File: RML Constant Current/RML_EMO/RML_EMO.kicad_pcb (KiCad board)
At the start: 2 copper layers, 72 x 34 mm, 50 parts, among them J1 Tyco, J2 NANOFIT-4PIN, J3 Tyco, Q3 Q_NMOS_GSD, Q4 Q_NMOS_GSD, Q5 Q_NMOS_GSD, U1 LR8K4-G, U2 LM555xM, U5 LM1117DT-5.0, U6 Optocoupler, U7 74AHC1G02, U8 OPA1662DGK

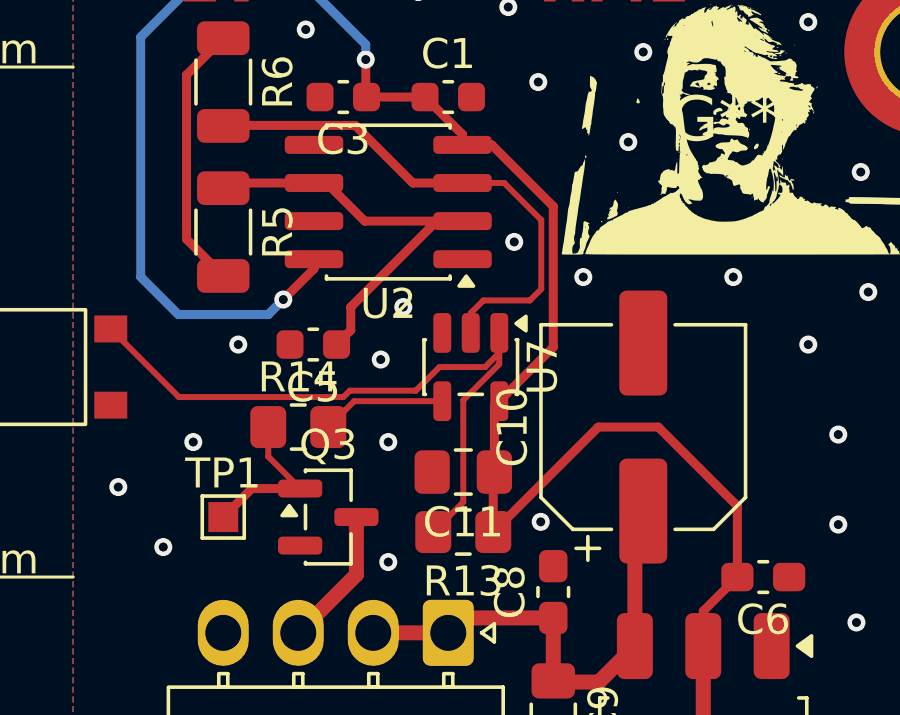
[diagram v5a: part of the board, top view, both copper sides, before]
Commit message: changed nor gate footprint to smaller footprint
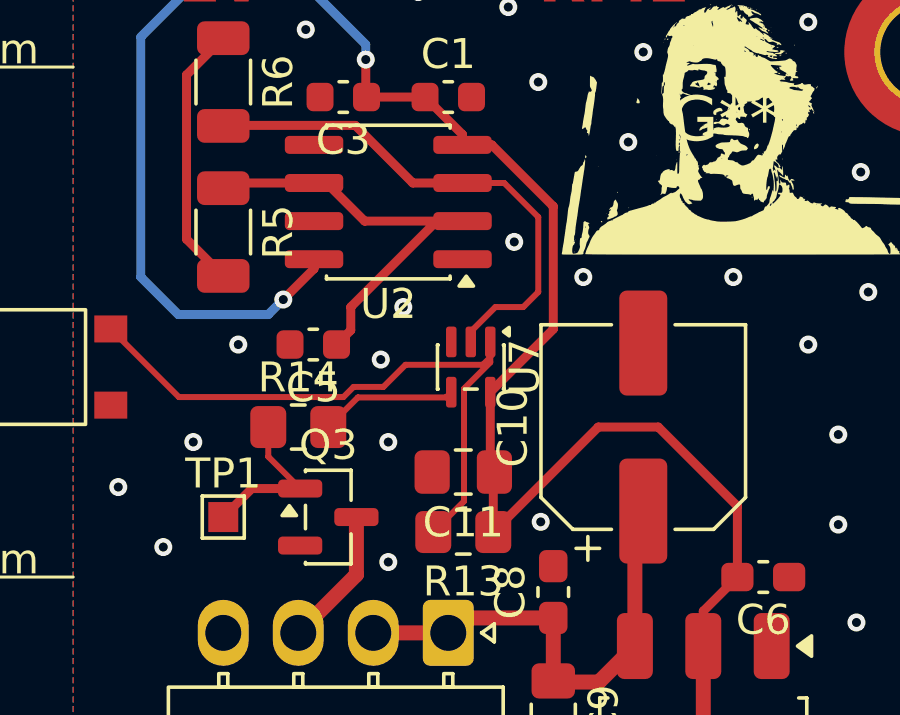
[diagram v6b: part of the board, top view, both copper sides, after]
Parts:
- U7: footprint Package_TO_SOT_SMD:SOT-23-5 -> Package_TO_SOT_SMD:SOT-353_SC-70-5
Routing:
- net Net-(R13-Pad2): track 22.7 -> 21.8 mm
- net CLOCK: track 18.1 -> 17.4 mm

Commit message: fixed NOR gate part #
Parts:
- U7: value 74AHC1G02 -> (none)
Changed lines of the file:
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@@
 			)
 		)
-		(property "Value" "74AHC1G02"
+		(property "Value" ""
 			(at 0 1.8 270)
 			(layer "F.Fab")
@@
 			)
 		)
-		(property "Mouser#" " 595-SN74AHC1G02DBE4 "
+		(property "Mouser#" "595-SN74AHC1G02DCG4"
 			(at 0 0 270)
 			(unlocked yes)
@@
 			)
 		)
-		(property "Manufacturer#" " SN74AHC1G02DBVRE4 "
+		(property "Manufacturer#" "SN74AHC1G02DCKRG4"
 			(at 0 0 270)
 			(unlocked yes)
